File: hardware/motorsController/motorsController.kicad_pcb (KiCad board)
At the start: 2 copper layers, 46 parts, among them J1 batery_connector, J2 Screw_Terminal_01x01, J3 Screw_Terminal_01x01, J4 Screw_Terminal_01x01, J5 Screw_Terminal_01x01, J6 Screw_Terminal_01x01, J7 Screw_Terminal_01x01, J8 Screw_Terminal_01x01, J9 Screw_Terminal_01x01, U1 VNH5019A-E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

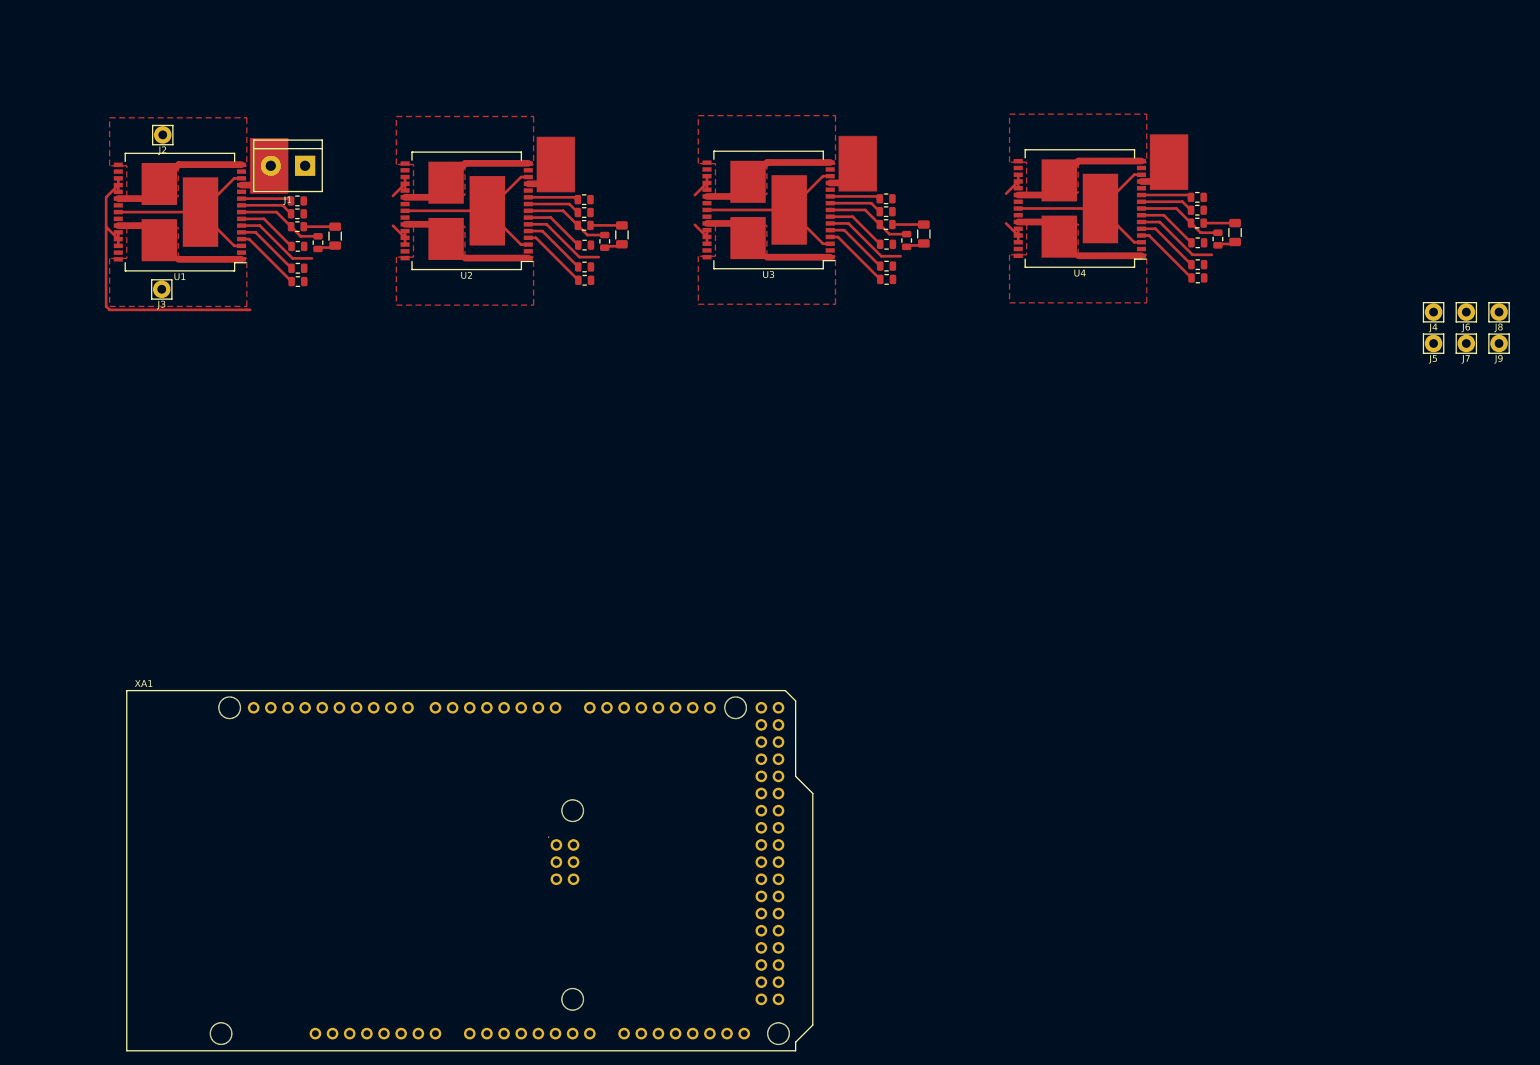
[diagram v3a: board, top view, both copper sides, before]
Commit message: layout and connect power for a pair of drivers
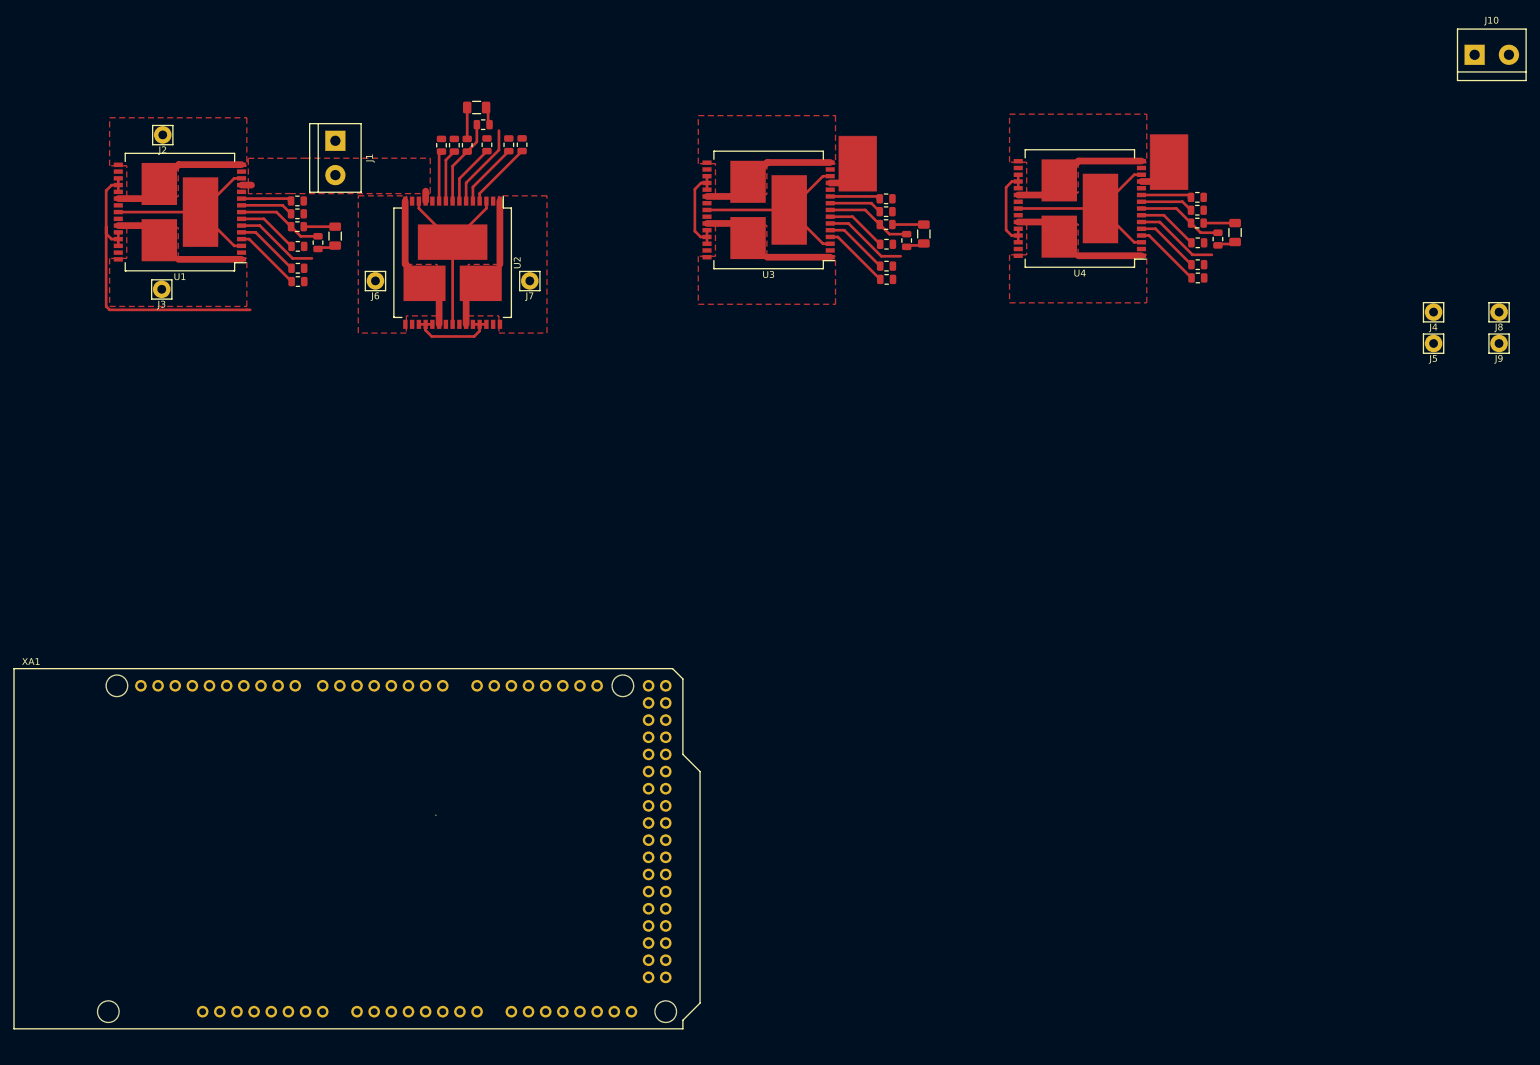
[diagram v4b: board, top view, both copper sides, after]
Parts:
- added J10: batery_connector, TerminalBlock:TerminalBlock_bornier-2_P5.08mm, F.Cu at (241.3, 26.2)
- moved J6 161.6 mm to (78.5, 59.7)
- moved J7 139.0 mm to (101.3, 59.7)
- moved C2 28.6 mm to (93.5, 34.0), turned to 180 degrees
- moved R8 25.0 mm to (94.4, 36.6), turned to 0 degrees
- moved R11 22.6 mm to (88.3, 39.6), turned to 90 degrees
- moved R10 22.1 mm to (100.2, 39.6), turned to 90 degrees
- moved R14 21.7 mm to (90.2, 39.6), turned to 90 degrees
- moved R13 21.3 mm to (98.2, 39.6), turned to 90 degrees
- moved R9 21.0 mm to (92.1, 39.6), turned to 90 degrees
- moved R12 20.7 mm to (95.0, 39.6), turned to 90 degrees
- moved XA1 17.0 mm to (25.0, 170.5)
- moved U2 7.97 mm to (89.9, 57.0), turned to 270 degrees
- moved J1 5.81 mm to (72.6, 39.0), turned to 270 degrees
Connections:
- J1 pad 2: /bat+ -> /bat_front+
- U1 pad 12: /bat+ -> /bat_front+
- U2 pad 12: /bat+ -> /bat_front+
- U3 pad 12: /bat+ -> /bat_rear+
- U4 pad 12: /bat+ -> /bat_rear+
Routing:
- net /bat+: track 22.1 -> 0.00 mm
- net GND: track 142.4 -> 160.1 mm
- net /bat_rear+: track 0.00 -> 11.0 mm
- net /bat_front+: track 0.00 -> 2.96 mm
- added copper zone on F.Cu, net /bat_front+

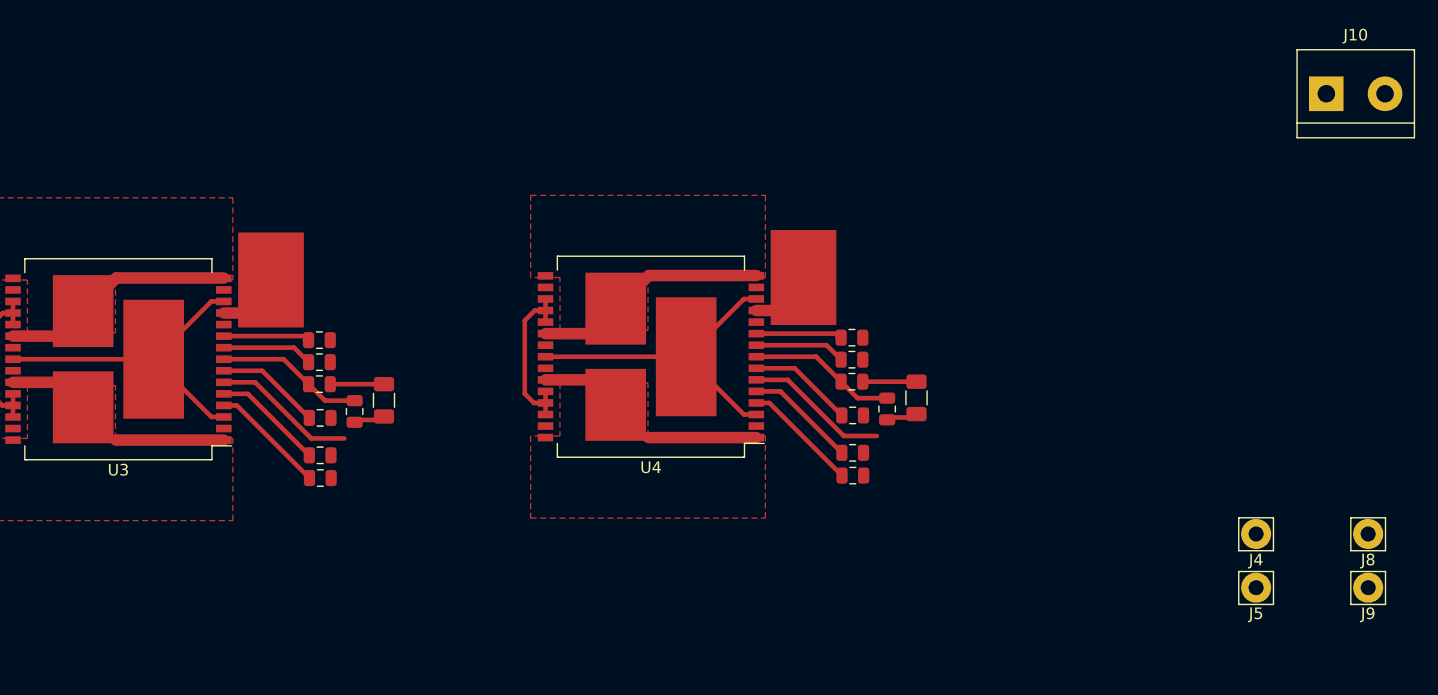
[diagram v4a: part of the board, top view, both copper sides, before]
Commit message: copy layout to the second pair of drivers
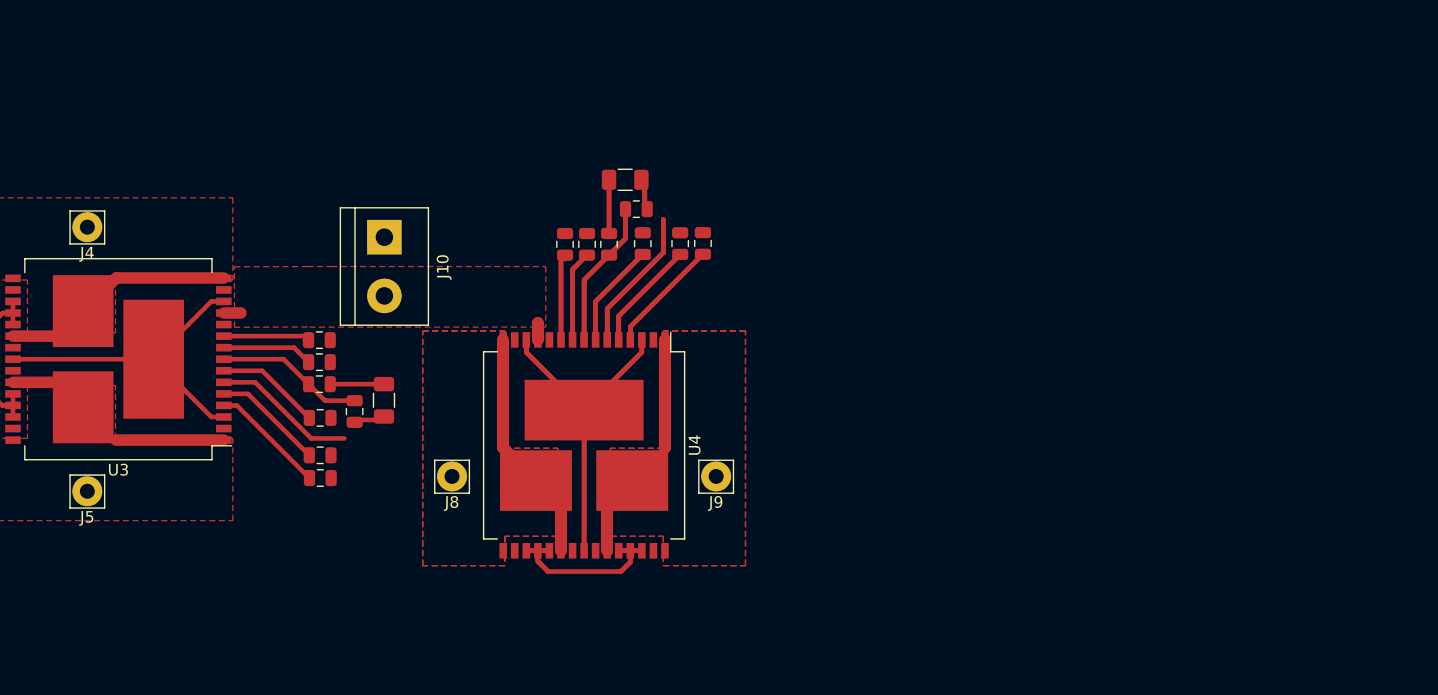
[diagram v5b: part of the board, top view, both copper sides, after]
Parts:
- moved J4 104.6 mm to (134.0, 37.8)
- moved J5 101.5 mm to (134.0, 60.6)
- moved J10 82.5 mm to (159.7, 38.7), turned to 270 degrees
- moved J8 79.5 mm to (165.6, 59.4)
- moved J9 57.3 mm to (188.5, 59.4)
- moved C4 31.5 mm to (180.6, 33.7), turned to 180 degrees
- moved R22 27.8 mm to (181.5, 36.2), turned to 0 degrees
- moved R25 26.1 mm to (175.4, 39.3), turned to 90 degrees
- moved R28 25.0 mm to (177.3, 39.3), turned to 90 degrees
- moved R23 24.2 mm to (179.2, 39.3), turned to 90 degrees
- moved R24 23.9 mm to (187.3, 39.2), turned to 90 degrees
- moved R26 23.5 mm to (182.1, 39.2), turned to 90 degrees
- moved R27 23.5 mm to (185.3, 39.2), turned to 90 degrees
- moved U4 9.61 mm to (177.0, 56.7), turned to 270 degrees
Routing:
- net +5V: track 113.9 -> 142.3 mm
- net GND: track 160.1 -> 185.5 mm
- net /sheet5F8B7956/out_b: track 20.3 -> 40.7 mm
- net /sheet5F8B7956/out_a: track 20.3 -> 40.6 mm
- net Net-(R22-Pad1): track 13.2 -> 26.5 mm
- net Net-(R24-Pad1): track 10.0 -> 20.0 mm
- net Net-(R27-Pad1): track 9.60 -> 19.2 mm
- net Net-(R26-Pad1): track 9.11 -> 18.2 mm
- net Net-(R28-Pad1): track 7.86 -> 15.7 mm
- net Net-(R25-Pad1): track 7.81 -> 15.6 mm
- net /bat_rear+: track 11.0 -> 4.44 mm
- net /motor_left_rear_cs: track 2.66 -> 5.33 mm
- added copper zone on F.Cu, net /bat_rear+

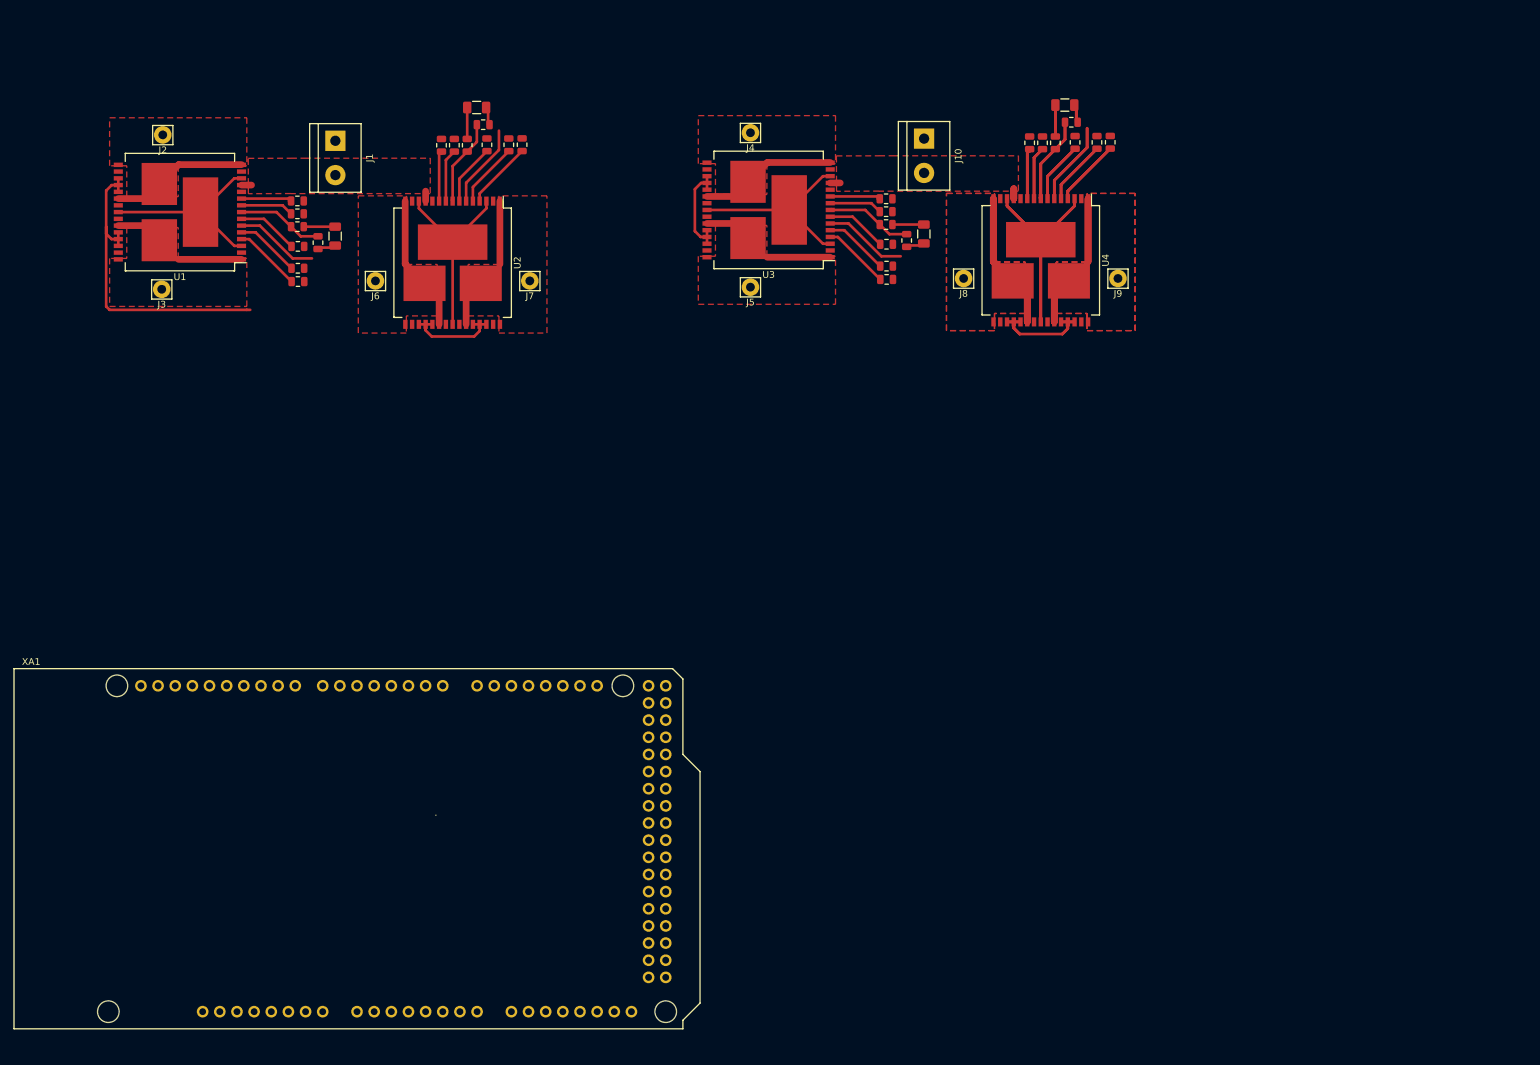
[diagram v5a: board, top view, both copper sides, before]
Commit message: create a board outline and start routing signal traces
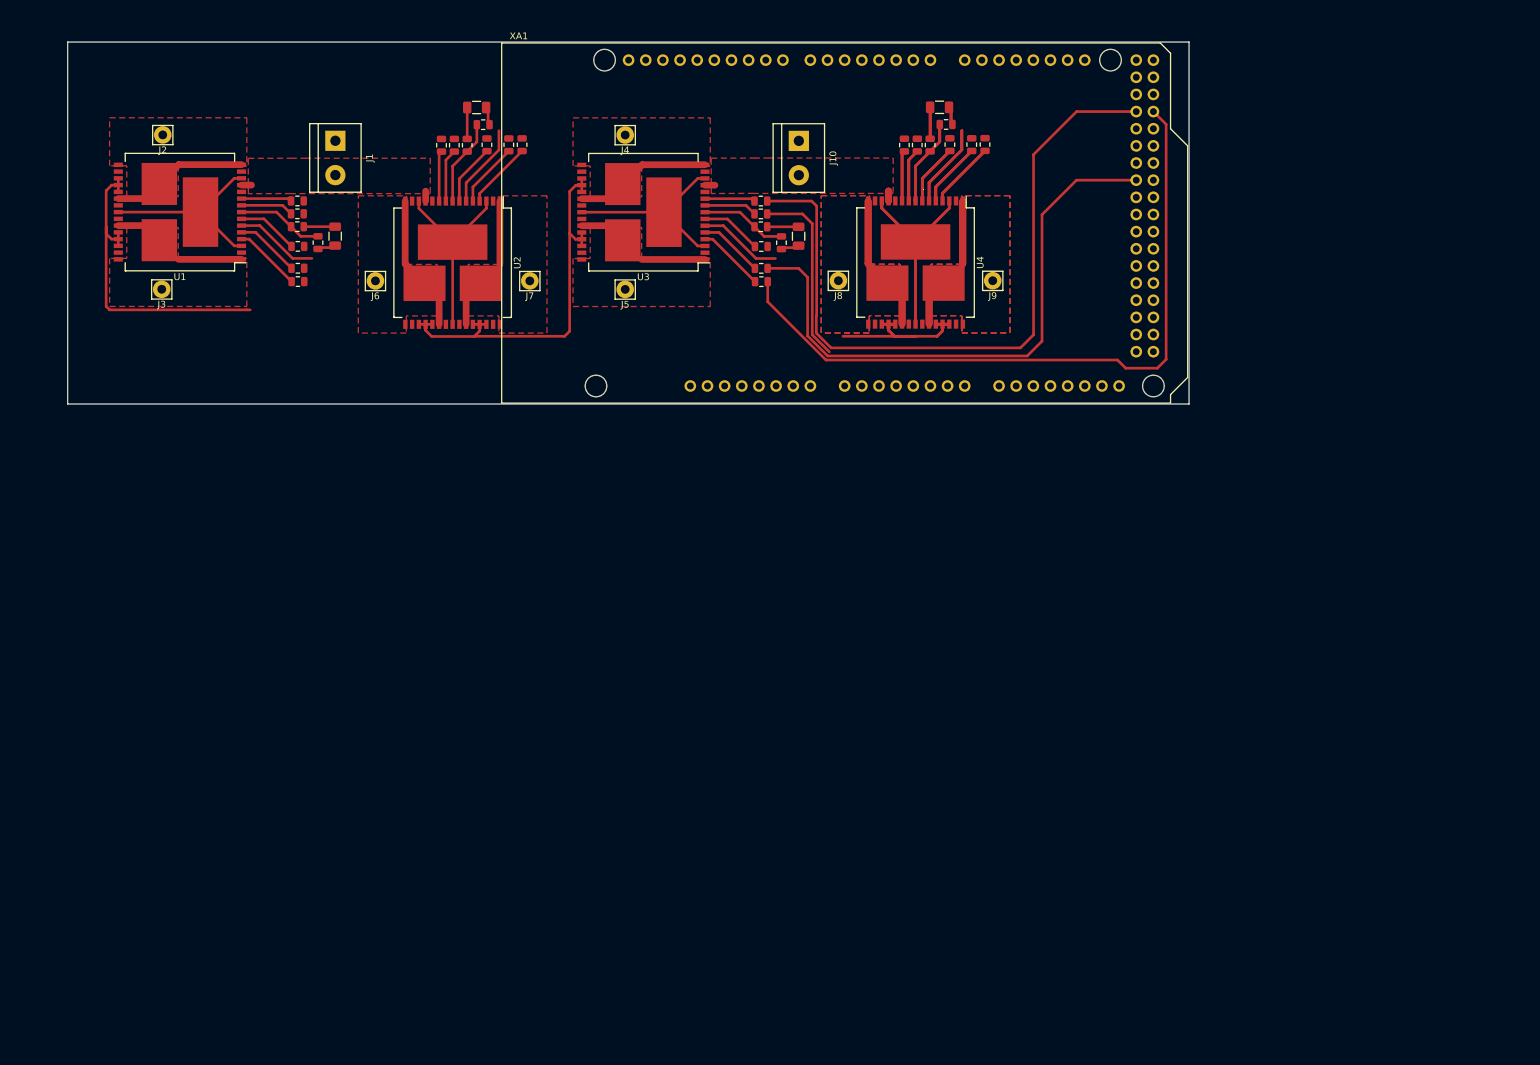
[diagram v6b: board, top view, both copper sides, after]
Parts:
- moved XA1 117.5 mm to (97.2, 77.8)
- moved J9 18.6 mm to (169.9, 59.7)
- moved R17 18.6 mm to (135.6, 59.8)
- moved R24 18.6 mm to (168.8, 39.5)
- moved C3 18.6 mm to (141.2, 53.1)
- moved C4 18.6 mm to (162.0, 34.0)
- moved J10 18.6 mm to (141.2, 39.0)
- moved J4 18.6 mm to (115.5, 38.1)
- moved J5 18.6 mm to (115.5, 61.0)
- moved J8 18.6 mm to (147.0, 59.7)
- moved R15 18.6 mm to (138.6, 54.1)
- moved R16 18.6 mm to (135.6, 51.7)
- moved R18 18.6 mm to (135.6, 47.9)
- moved R19 18.6 mm to (135.6, 54.6)
- moved R20 18.6 mm to (135.6, 57.9)
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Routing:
- net /motor_right_rear_back: track 0.00 -> 104.9 mm
- net /motor_right_rear_fwd: track 0.00 -> 104.1 mm
- net /motor_right_rear_diag_a: track 0.00 -> 86.8 mm
- net GND: track 185.5 -> 225.3 mm
- net /motor_right_rear_diag_b: track 0.00 -> 27.3 mm
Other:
- board outline added: 166.1 x 53.6 mm
